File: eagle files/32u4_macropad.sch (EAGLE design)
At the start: 89 parts, among them IC1 IS31FL3733-TQLS4, J1 TYPE-C-31-M-12, Q1 16Mhz, SW2 SWITCH-SMD-EVP-BB2A9B00, U1 ATMEGA32U4-TQFP44

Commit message: ESD Finished, led driver work, board placement work
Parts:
- removed F17: 1206L012, polyfuse-smd_10:1206L012
- added C14: 0.1uF, Components:CAPACITOR-0603
- added C8: 0.47uF, Components:CAPACITOR-0603
- added FB1, FB2: FERRITE_BEAD, Filter:FBCHIP-0603(1608-METRIC)
- added FUSE: 0603L050, polyfuse-smd_20:0603L050
- added RESET: 20k, Components:RESISTOR-0603
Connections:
- net INTBUSE?? renamed INTBUSE
- removed net N$27: R8.2, U1.D-
- new net 1: C14.1, C8.1
- new net N$14: J1.DP2, R8.1
- new net N$16: J1.DN2, R7.1
- new net N$18: R8.2
- new net N$19: R7.2
- new net N$22: FB2.1, J1.SHIELD
- new net N$24: FB1.2, FUSE.2
- new net VCC1: C14.2, C8.2, IC1.PVCC_1
- net 0: now also FB2.2, IC1.ADDR1, IC1.ADDR2, RESET.2; no longer J1.SHIELD
- net AUDIO: now also U1.PB6(PCINT6/OC1B/OC4B/ADC13); no longer U1.PB7(PCINT7/OC0A/OC1C/!RTS)
- net D+: now also U1.D+; no longer J1.DP2, R8.1
- net D-: now also U1.D-; no longer J1.DN2, R7.1
- net N$26: now also IC1.RSET, RESET.1; no longer R7.2, U1.D+
- net VCC: now also FUSE.1; no longer F17.1, IC1.PVCC_1
- net VUSB: now also FB1.1; no longer F17.2
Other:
- moved on the sheet: C1, C10, C11, C12, C13, C15, C18, C19, C2, C20, C21, C3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

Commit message: Led driver finished, usb footprint made unilateral and fixed D+ D- connection, board work
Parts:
- removed R10, R9: 100k, Components:RESISTOR-0603
- R5, R6: value 1k -> 4.7k
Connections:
- removed net INTBUSE: IC1.INTB, R9.1
- removed net N$16: J1.DN2, R7.1
- removed net N$19: R7.2
- net 0: no longer R10.2
- net D+: now also R8.2; no longer J1.DP1
- net D-: now also R7.2; no longer J1.DN1
- net N$14: now also J1.DN1, J1.DN2, R7.1; no longer J1.DP2, R8.1
- net N$18: now also J1.DP1, J1.DP2, R8.1; no longer R8.2
- net SDB: no longer IC1.SDB, R10.1
- net VCC: now also IC1.SDB; no longer R9.2
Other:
- note added: "LED DRIVER"
- moved on the sheet: C14, C15, C18, C19, C20, C21, C3, C4, C5, C7, C8, D0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

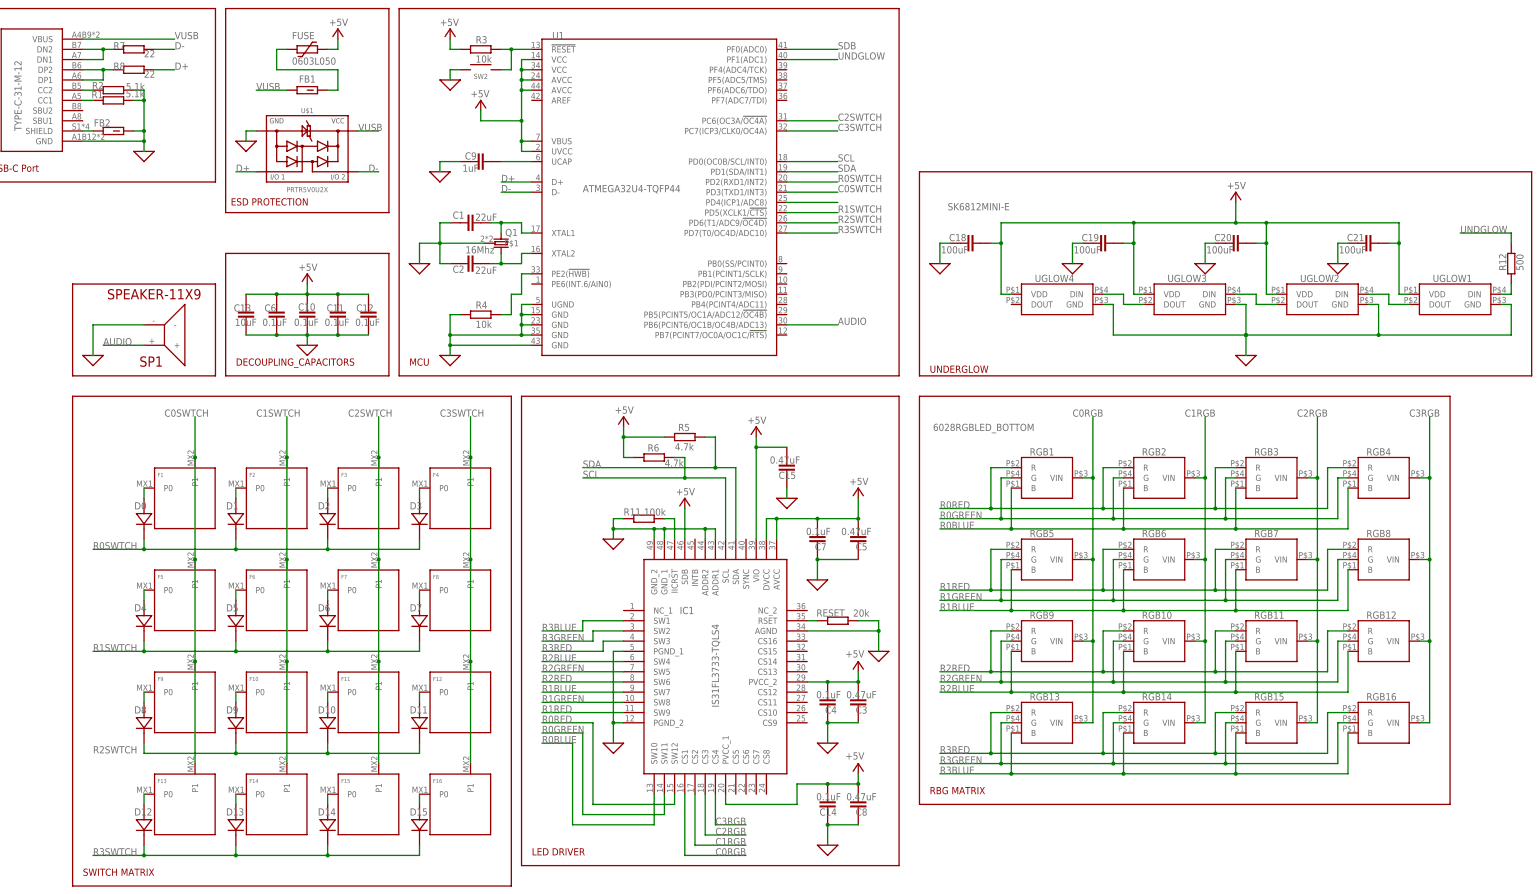
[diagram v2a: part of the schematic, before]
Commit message: Major board routing, GND net fix
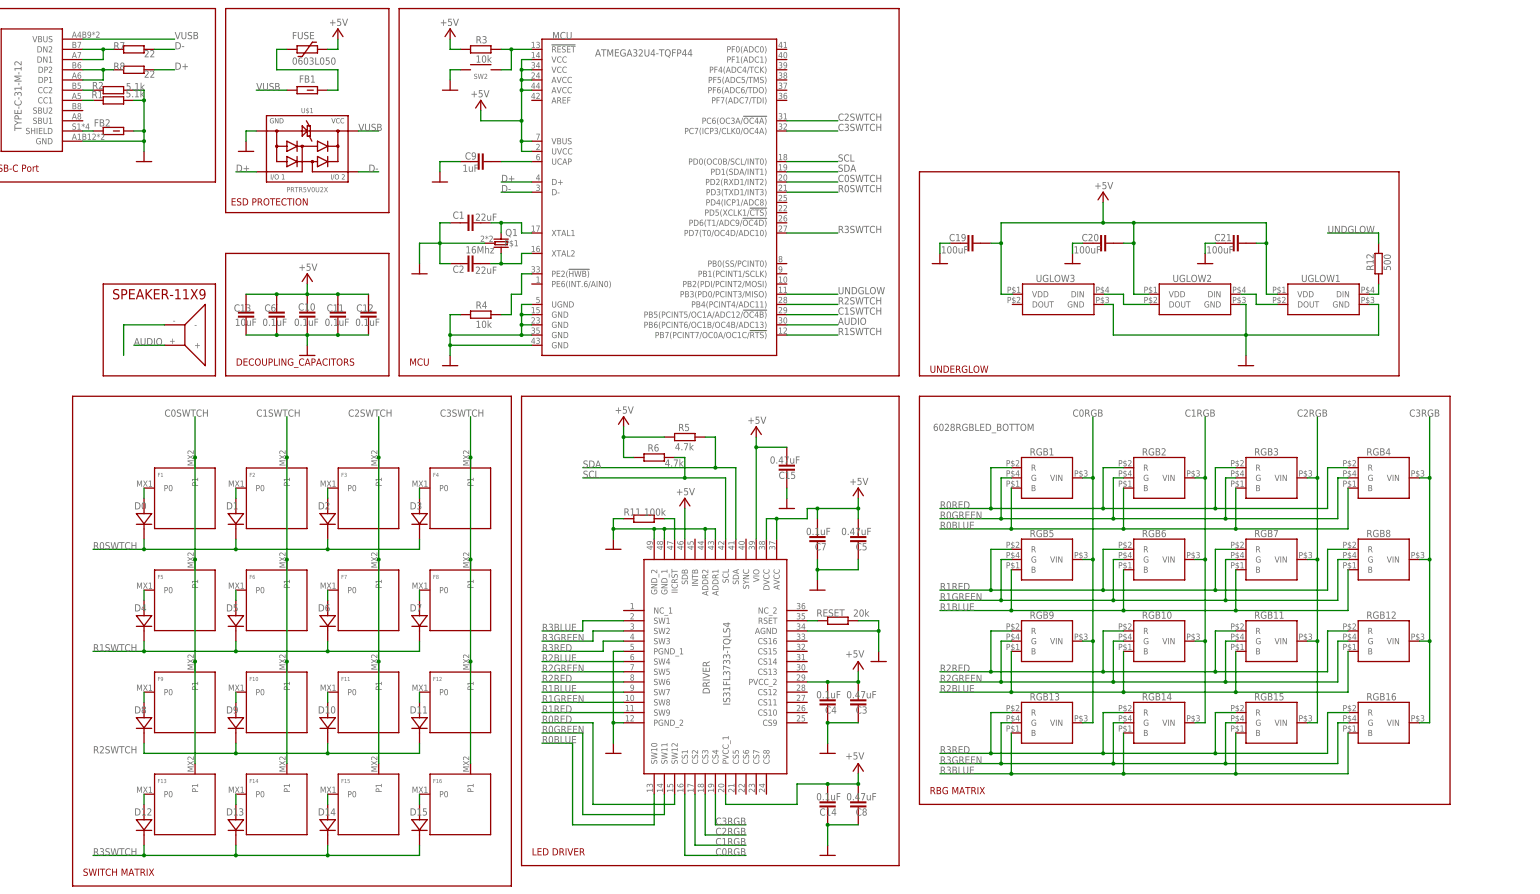
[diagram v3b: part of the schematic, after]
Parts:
- removed C18: 100uF, Components:CAPACITOR-0603
- removed UGLOW4: SK6812MINI-E, SK6812MINI-E:SK6812MINI-E
- renumbered IC1 to DRIVER, U1 to MCU
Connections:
- removed net 0: C1.1, C10.2, C11.2, C12.2, C13.2, C15.1, C18.1, C19.1, C2.1, C20.1, C21.1, C3.1, C4.1, C5.1, C6.2, C7.1, C9.1, DRIVER.ADDR1, DRIVER.ADDR2, DRIVER.AGND, DRIVER.GND_1, DRIVER.GND_2, DRIVER.PGND_1, DRIVER.PGND_2, FB2.2, J1.GND, MCU.GND@1, MCU.GND@2, MCU.GND@3, MCU.GND@4, MCU.UGND, Q1.P$1, R1.1, R11.1, R2.1, R4.1, RESET.2, SP1.-, SW2.1, U$1.1, UGLOW1.GND, UGLOW2.GND, UGLOW3.GND, UGLOW4.GND
- removed net 1: C14.1, C8.1
- removed net N$6: UGLOW3.DOUT, UGLOW4.DIN
- removed net SDB: MCU.PF0(ADC0)
- new net GND: C1.1, C10.2, C11.2, C12.2, C13.2, C14.1, C15.1, C19.1, C2.1, C20.1, C21.1, C3.1, C4.1, C5.1, C6.2, C7.1, C8.1, C9.1, DRIVER.ADDR1, DRIVER.ADDR2, DRIVER.AGND, DRIVER.GND_1, DRIVER.GND_2, DRIVER.PGND_1, DRIVER.PGND_2, FB2.2, J1.GND, MCU.GND@1, MCU.GND@2, MCU.GND@3, MCU.GND@4, MCU.UGND, Q1.P$1, R1.1, R11.1, R2.1, R4.1, RESET.2, SW2.1, U$1.1, UGLOW1.GND, UGLOW2.GND, UGLOW3.GND
- new net N$40: SP1.-
- net C0SWTCH: now also MCU.PD2(RXD1/INT2); no longer MCU.PD3(TXD1/INT3)
- net C1SWTCH: now also MCU.PB5(PCINT5/OC1A/ADC12/!OC4B); no longer MCU.PD4(ICP1/ADC8)
- net R0SWTCH: now also MCU.PD3(TXD1/INT3); no longer MCU.PD2(RXD1/INT2)
- net R1SWTCH: now also MCU.PB7(PCINT7/OC0A/OC1C/!RTS); no longer MCU.PD5(XCLK1/!CTS)
- net R2SWTCH: now also MCU.PB4(PCINT4/ADC11); no longer MCU.PD6(T1/ADC9/!OC4D)
- net UNDGLOW: now also MCU.PB3(PD0/PCINT3/MISO); no longer MCU.PF1(ADC1)
- net VCC: no longer C18.2, UGLOW4.VDD
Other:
- moved on the sheet: C19, C20, C21, R12, UGLOW1, UGLOW2, UGLOW3

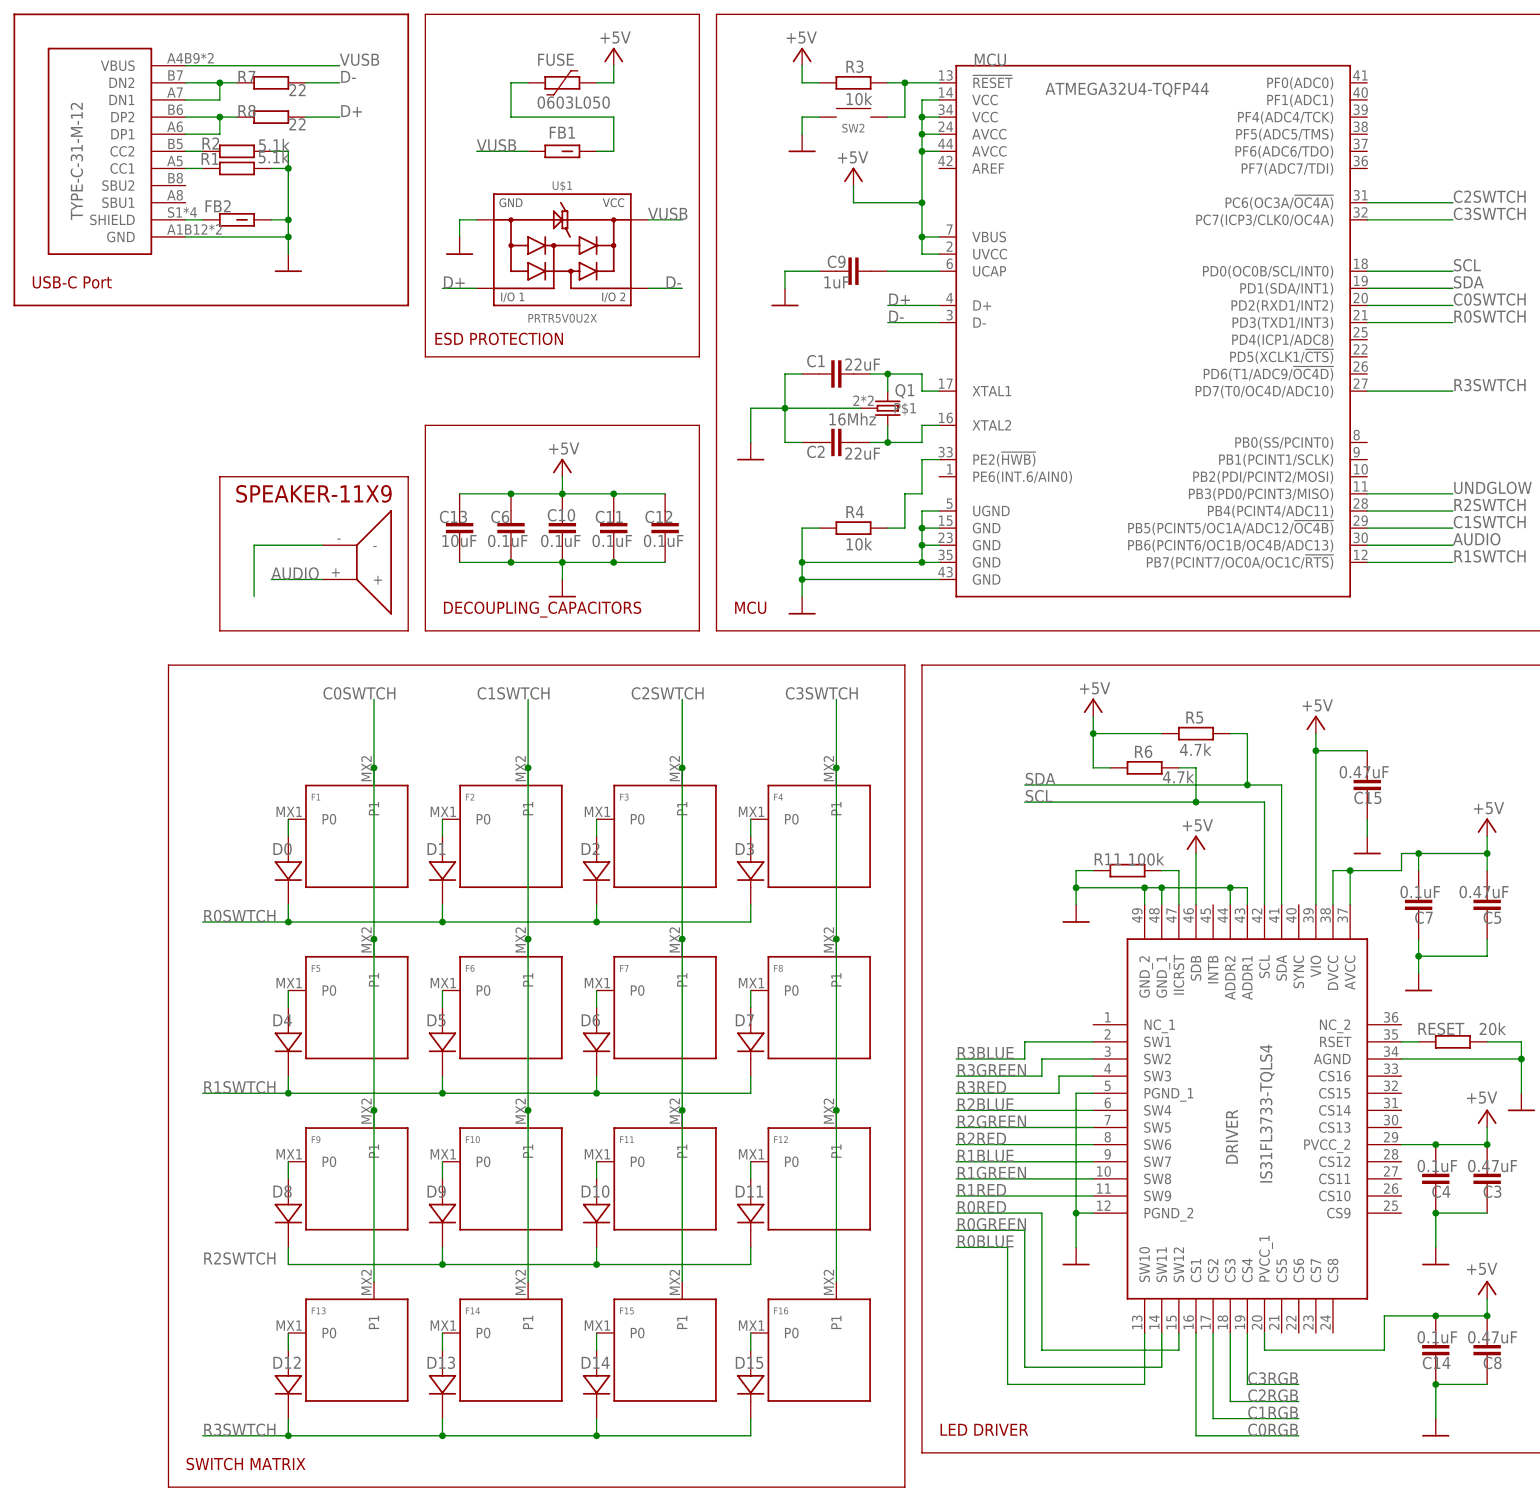
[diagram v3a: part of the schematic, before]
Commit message: Board USB are work, minor fixes
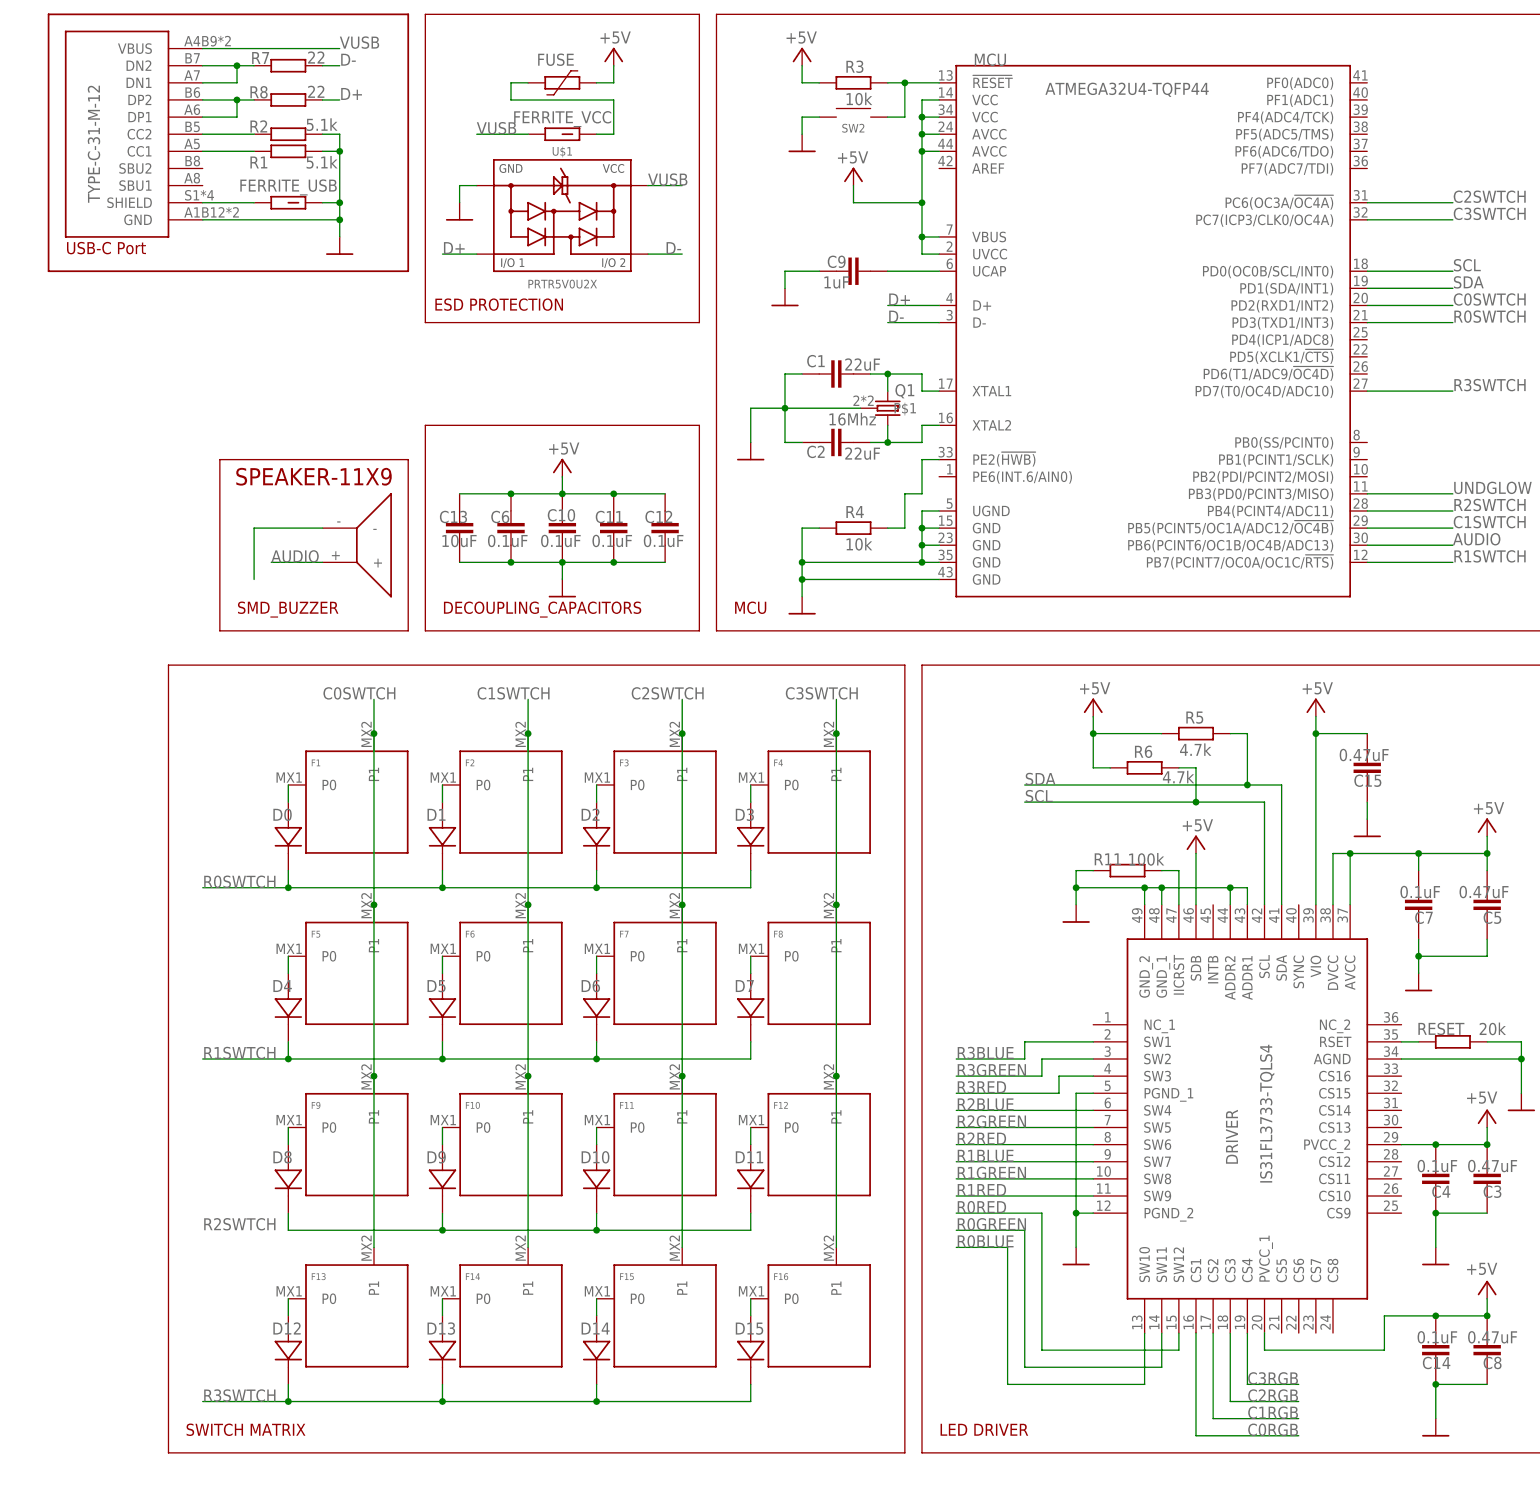
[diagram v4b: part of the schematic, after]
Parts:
- removed FB1, FB2: FERRITE_BEAD, Filter:FBCHIP-0603(1608-METRIC)
- added FERRITE_USB, FERRITE_VCC: FERRITE_BEAD, Filter:FBCHIP-0603(1608-METRIC)
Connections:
- removed net N$15: J1.CC2, R2.2
- removed net N$2: J1.CC1, R1.2
- removed net N$22: FB2.1, J1.SHIELD
- new net VBUS: FERRITE_VCC.2, FUSE.2
- net GND: now also FERRITE_USB.2; no longer C1.1, C10.2, C11.2, C12.2, C13.2, C14.1, C15.1, C19.1, C2.1, C20.1, C21.1, C3.1, C4.1, C5.1, C6.2, C7.1, C8.1, C9.1, DRIVER.ADDR1, DRIVER.ADDR2, DRIVER.AGND, DRIVER.GND_1, DRIVER.GND_2, DRIVER.PGND_1, DRIVER.PGND_2, FB2.2, Q1.P$1, R11.1, RESET.2, SW2.1, U$1.1, UGLOW1.GND, UGLOW2.GND, UGLOW3.GND
- net N$24: now also C1.1, C10.2, C11.2, C12.2, C13.2, C14.1, C15.1, C19.1, C2.1, C20.1, C21.1, C3.1, C4.1, C5.1, C6.2, C7.1, C8.1, C9.1, DRIVER.ADDR1, DRIVER.ADDR2, DRIVER.AGND, DRIVER.GND_1, DRIVER.GND_2, DRIVER.PGND_1, DRIVER.PGND_2, FERRITE_USB.1, J1.CC1, J1.CC2, J1.SHIELD, Q1.P$1, R1.2, R11.1, R2.2, RESET.2, SW2.1, U$1.1, UGLOW1.GND, UGLOW2.GND, UGLOW3.GND; no longer FB1.2, FUSE.2
- net VUSB: now also FERRITE_VCC.1; no longer FB1.1
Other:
- note added: "SMD_BUZZER"
- moved on the sheet: C15, D0, D1, D10, D11, D12, D13, D14, D15, D2, D3, D4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

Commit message: GND net fixes, drc checks, other fixes
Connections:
- removed net N$40: SP1.-
- removed net VUSB: FERRITE_VCC.1, J1.VBUS, U$1.4
- new net N$2: FERRITE_VCC.1, FUSE.1
- net GND: now also C1.1, C10.2, C11.2, C12.2, C13.2, C14.1, C15.1, C19.1, C2.1, C20.1, C21.1, C3.1, C4.1, C5.1, C6.2, C7.1, C8.1, C9.1, DRIVER.ADDR1, DRIVER.ADDR2, DRIVER.AGND, DRIVER.GND_1, DRIVER.GND_2, DRIVER.PGND_1, DRIVER.PGND_2, Q1.P$1, R11.1, RESET.2, SP1.-, SW2.1, U$1.1, UGLOW1.GND, UGLOW2.GND, UGLOW3.GND
- net N$24: no longer C1.1, C10.2, C11.2, C12.2, C13.2, C14.1, C15.1, C19.1, C2.1, C20.1, C21.1, C3.1, C4.1, C5.1, C6.2, C7.1, C8.1, C9.1, DRIVER.ADDR1, DRIVER.ADDR2, DRIVER.AGND, DRIVER.GND_1, DRIVER.GND_2, DRIVER.PGND_1, DRIVER.PGND_2, Q1.P$1, R11.1, RESET.2, SW2.1, U$1.1, UGLOW1.GND, UGLOW2.GND, UGLOW3.GND
- net VBUS: now also J1.VBUS, U$1.4; no longer FERRITE_VCC.2
- net VCC: now also FERRITE_VCC.2; no longer FUSE.1
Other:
- moved on the sheet: C19, C20, C21, FERRITE_USB, FERRITE_VCC, FUSE, R1, R12, R2, R7, R8

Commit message: ESD routing fix and finished, usb data line resistors moved after ESD, minor fixes
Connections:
- removed net N$14: J1.DN1, J1.DN2, R7.1
- removed net N$18: J1.DP1, J1.DP2, R8.1
- new net N$15: MCU.D+, R7.2
- new net N$6: MCU.D-, R8.2
- net D+: now also J1.DP1, J1.DP2, R7.1, U$1.3; no longer MCU.D+, R8.2, U$1.2
- net D-: now also J1.DN1, J1.DN2, R8.1, U$1.2; no longer MCU.D-, R7.2, U$1.3
- net GND: now also UGLOW3.DOUT
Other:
- moved on the sheet: C20, R7, R8

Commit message: Routing fixes
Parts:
- removed UGLOW3: SK6812MINI-E, SK6812MINI-E:SK6812MINI-E
- added C16: 100nF, Components:CAPACITOR-0603
- added SK6812MINI-E: SK6812MINI-E, SK6812MINI-E:SK6812MINI-E
- C19, C20, C21: value 100uF -> 100nF
- Q1: value 16Mhz -> 16MHz
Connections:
- removed net VCC1: C14.2, C8.2, DRIVER.PVCC_1
- net AUDIO: now also C16.1, MCU.PC6(OC3A/!OC4A); no longer MCU.PB6(PCINT6/OC1B/OC4B/ADC13)
- net C2SWTCH: now also MCU.PB6(PCINT6/OC1B/OC4B/ADC13); no longer MCU.PC6(OC3A/!OC4A)
- net GND: now also C16.2, SK6812MINI-E.GND; no longer UGLOW3.DOUT, UGLOW3.GND
- net N$25: now also SK6812MINI-E.DIN; no longer UGLOW3.DIN
- net VCC: now also C14.2, C8.2, DRIVER.PVCC_1, SK6812MINI-E.VDD; no longer UGLOW3.VDD
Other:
- note added: "USB-C PORT"
- note removed: "USB-C Port"
- moved on the sheet: C1, C10, C11, C12, C13, C19, C2, C20, C21, C6, FERRITE_USB, FERRITE_VCC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
